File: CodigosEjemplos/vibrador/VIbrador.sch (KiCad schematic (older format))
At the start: 5 parts, among them U1 Pila3,7V, U2 ArduinoNANO, U3 Buzzer, U4 HC-05, U5 Buzzer

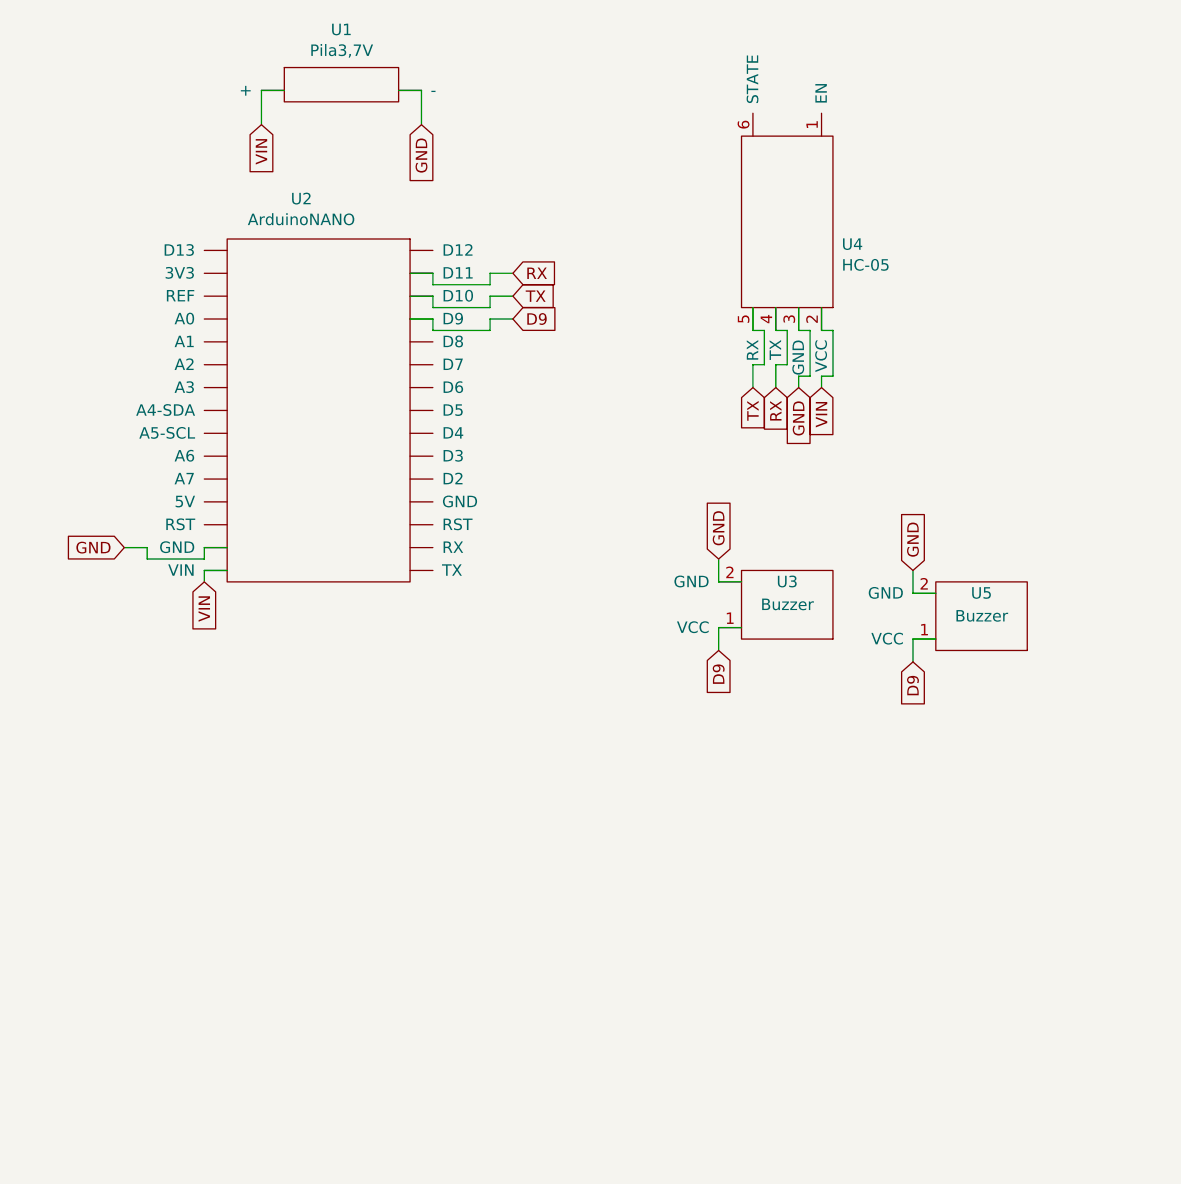
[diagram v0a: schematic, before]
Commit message: Se agregaron los PCB de HC-05, pila (falta completar) y vibrador
Tambien cambie el simbolo de hc-05 ya que le faltaban dos pines
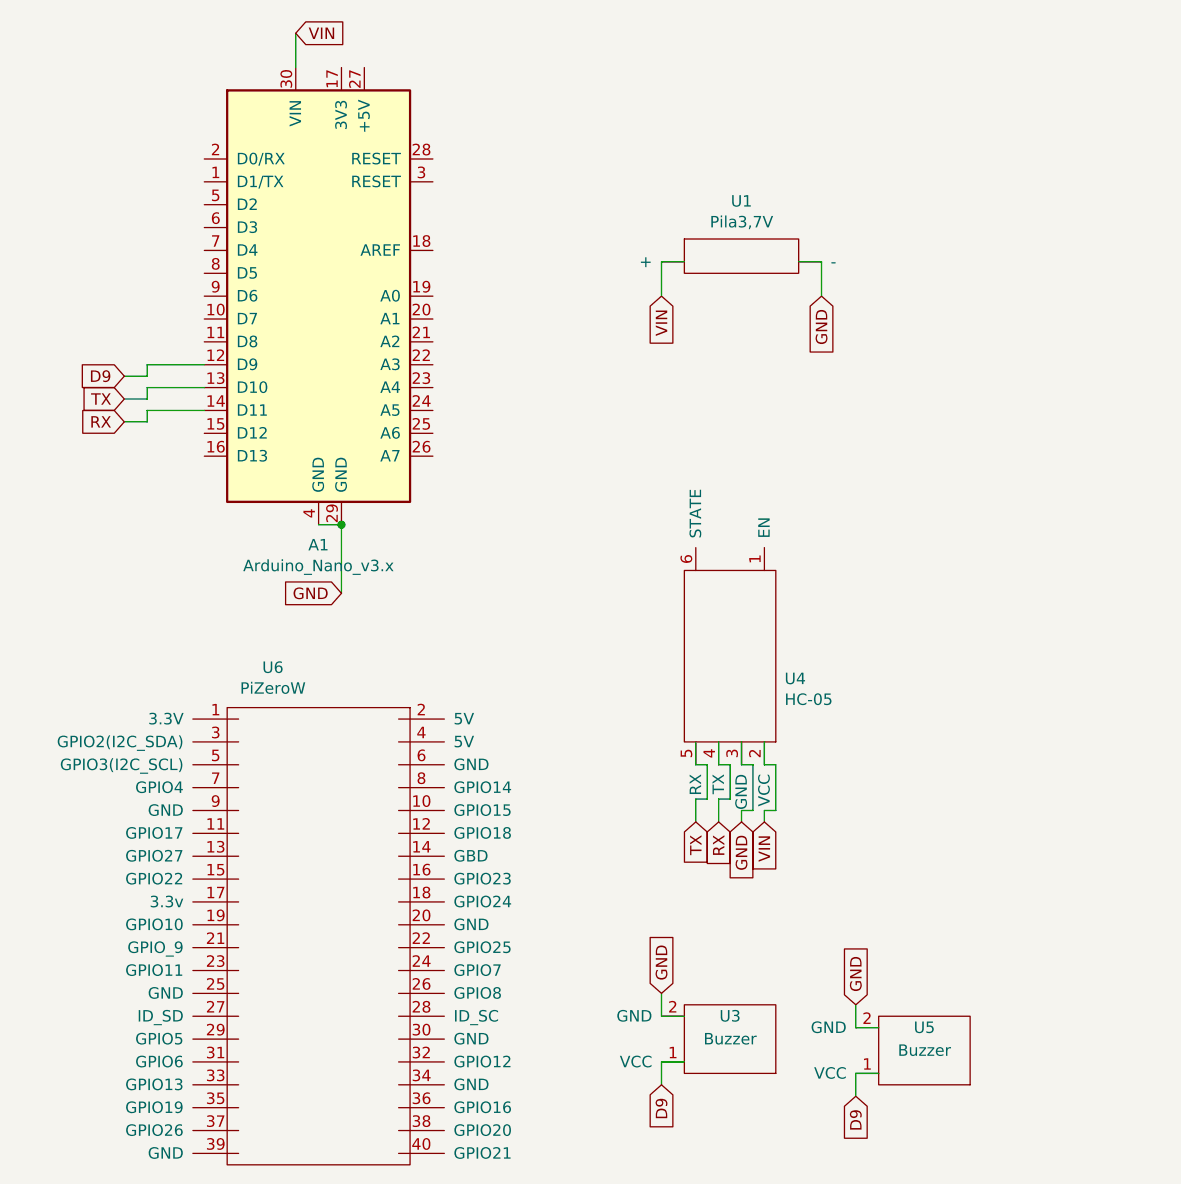
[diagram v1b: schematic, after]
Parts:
- removed U2: ArduinoNANO, Connector_PinHeader_2.54mm:PinHeader_1x15_P2.54mm_Vertical, symbol VIbrador-rescue:ArduinoNANO-Modulos-VIbrador-rescue
- added A1: Arduino_Nano_v3.x, Module:Arduino_Nano, symbol MCU_Module:Arduino_Nano_v3.x
- added U6: PiZeroW, Module:Raspberry_Pi_Zero_Socketed_THT_FaceDown_MountingHoles, symbol VIbrador-rescue:PiZeroW
- U1: footprint (none) -> VibradorPCB:Pila de Litio
- U3, U5: footprint Connector_PinHeader_2.54mm:PinHeader_1x02_P2.54mm_Vertical -> VibradorPCB:Vibrador
- U4: footprint Connector_PinHeader_2.54mm:PinHeader_1x06_P2.54mm_Vertical -> VibradorPCB:HC-05
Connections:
- net D9: now also A1.12 (D9)
- net GND: now also A1.29 (GND), A1.4 (GND)
- net RX: now also A1.14 (D11)
- net TX: now also A1.13 (D10)
- net VIN: now also A1.30 (VIN)
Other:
- moved on the sheet: U1, U3, U4, U5
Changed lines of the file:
@@
 EESchema Schematic File Version 4
-EELAYER 30 0
+LIBS:VIbrador-cache
+EELAYER 29 0
 EELAYER END
 $Descr A4 8268 11693 portrait
@@
 L VIbrador-rescue:HC-05-Modulos-VIbrador-rescue U4
 U 1 1 5E6EC1C3
-P 5000 2200
-F 0 "U4" V 5074 2338 50  0000 L CNN
-F 1 "HC-05" V 5165 2338 50  0000 L CNN
-F 2 "Connector_PinHeader_2.54mm:PinHeader_1x06_P2.54mm_Vertical" H 5000 2200 50  0001 C CNN
-F 3 "" H 5000 2200 50  0001 C CNN
-	1    5000 2200
+P 4750 4100
+F 0 "U4" V 4824 4238 50  0000 L CNN
+F 1 "HC-05" V 4915 4238 50  0000 L CNN
+F 2 "VibradorPCB:HC-05" H 4750 4100 50  0001 C CNN
+F 3 "" H 4750 4100 50  0001 C CNN
+	1    4750 4100
 	0    1    1    0
 $EndComp
@@
 L VIbrador-rescue:Pila3,7V-Modulos-VIbrador-rescue U1
 U 1 1 5E6ECDF3
-P 2900 1550
-F 0 "U1" H 2950 1765 50  0000 C CNN
-F 1 "Pila3,7V" H 2950 1674 50  0000 C CNN
-F 2 "" H 2900 1550 50  0001 C CNN
-F 3 "" H 2900 1550 50  0001 C CNN
-	1    2900 1550
+P 4650 2300
+F 0 "U1" H 4700 2515 50  0000 C CNN
+F 1 "Pila3,7V" H 4700 2424 50  0000 C CNN
+F 2 "VibradorPCB:Pila de Litio" H 4650 2300 50  0001 C CNN
+F 3 "" H 4650 2300 50  0001 C CNN
+	1    4650 2300
 	1    0    0    -1
 $EndComp
-Text GLabel 2600 1750 3    50   Input ~ 0
+Text GLabel 4350 2500 3    50   Input ~ 0
 VIN
-Text GLabel 3300 1750 3    50   Input ~ 0
-GND
-Wire Wire Line
-	3300 1750 3300 1600
-Wire Wire Line
-	3300 1600 3200 1600
-Wire Wire Line
-	2700 1600 2600 1600
-Wire Wire Line
-	2600 1600 2600 1750
-Text GLabel 2350 3750 3    50   Input ~ 0
+Text GLabel 5050 2500 3    50   Input ~ 0
+GND
+Wire Wire Line
+	5050 2500 5050 2350
+Wire Wire Line
+	5050 2350 4950 2350
+Wire Wire Line
+	4450 2350 4350 2350
+Wire Wire Line
+	4350 2350 4350 2500
+Text GLabel 2750 1350 2    50   Input ~ 0
 VIN
-Wire Wire Line
-	2450 3700 2350 3700
-Wire Wire Line
-	2350 3700 2350 3750
-Text GLabel 2000 3600 0    50   Input ~ 0
-GND
-Text GLabel 4750 2900 3    50   Input ~ 0
+Text GLabel 2950 3800 0    50   Input ~ 0
+GND
+Text GLabel 4500 4800 3    50   Input ~ 0
 TX
-Text GLabel 4850 2900 3    50   Input ~ 0
+Text GLabel 4600 4800 3    50   Input ~ 0
 RX
-Text GLabel 4600 4050 3    50   Input ~ 0
+Text GLabel 4350 5950 3    50   Input ~ 0
 D9
 Wire Wire Line
-	4700 3950 4600 3950
-Wire Wire Line
-	4600 3950 4600 4050
-Text GLabel 4600 3650 1    50   Input ~ 0
-GND
-Wire Wire Line
-	4600 3750 4600 3650
-Wire Wire Line
-	4600 3750 4700 3750
-Text GLabel 5050 2900 3    50   Input ~ 0
+	4450 5850 4350 5850
+Wire Wire Line
+	4350 5850 4350 5950
+Text GLabel 4350 5550 1    50   Input ~ 0
+GND
+Wire Wire Line
+	4350 5650 4350 5550
+Wire Wire Line
+	4350 5650 4450 5650
+Text GLabel 4800 4800 3    50   Input ~ 0
 VIN
-Text GLabel 4950 2900 3    50   Input ~ 0
-GND
-Text GLabel 3700 2400 2    50   Input ~ 0
+Text GLabel 4700 4800 3    50   Input ~ 0
+GND
+Text GLabel 2000 3050 0    50   Input ~ 0
 RX
-$Comp
-L VIbrador-rescue:ArduinoNANO-Modulos-VIbrador-rescue U2
-U 1 1 5E6EAAF3
-P 3100 2700
-F 0 "U2" V 2475 2375 50  0000 C CNN
-F 1 "ArduinoNANO" V 2566 2375 50  0000 C CNN
-F 2 "Connector_PinHeader_2.54mm:PinHeader_1x15_P2.54mm_Vertical" H 3100 2700 50  0001 C CNN
-F 3 "" H 3100 2700 50  0001 C CNN
-	1    3100 2700
-	0    1    1    0
-$EndComp
-Wire Wire Line
-	3250 2400 3350 2400
-Wire Wire Line
-	3600 2400 3700 2400
-Text GLabel 3700 2500 2    50   Input ~ 0
+Wire Wire Line
+	2100 3050 2000 3050
+Text GLabel 2000 2950 0    50   Input ~ 0
 TX
-Text GLabel 3700 2600 2    50   Input ~ 0
+Text GLabel 2000 2850 0    50   Input ~ 0
 D9
 Wire Wire Line
-	3600 2400 3600 2450
-Wire Wire Line
-	3600 2450 3350 2450
-Wire Wire Line
-	3350 2450 3350 2400
-Wire Wire Line
-	3350 2500 3350 2550
-Wire Wire Line
-	3350 2550 3600 2550
-Wire Wire Line
-	3600 2550 3600 2500
-Wire Wire Line
-	3600 2500 3700 2500
-Wire Wire Line
-	3700 2600 3600 2600
-Wire Wire Line
-	3600 2600 3600 2650
-Wire Wire Line
-	3600 2650 3350 2650
-Wire Wire Line
-	3350 2650 3350 2600
-Wire Wire Line
-	3350 2600 3250 2600
-Wire Wire Line
-	3250 2500 3350 2500
-Wire Wire Line
-	2450 3600 2350 3600
-Wire Wire Line
-	2350 3600 2350 3650
-Wire Wire Line
-	2350 3650 2100 3650
-Wire Wire Line
-	2100 3650 2100 3600
-Wire Wire Line
-	2100 3600 2000 3600
-Wire Wire Line
-	4750 2550 4750 2650
-Wire Wire Line
-	4750 2650 4800 2650
-Wire Wire Line
-	4800 2650 4800 2800
-Wire Wire Line
-	4800 2800 4750 2800
-Wire Wire Line
-	4750 2800 4750 2900
-Wire Wire Line
-	4850 2900 4850 2800
-Wire Wire Line
-	4850 2800 4900 2800
-Wire Wire Line
-	4900 2800 4900 2650
-Wire Wire Line
-	4900 2650 4850 2650
-Wire Wire Line
-	4850 2650 4850 2550
-Wire Wire Line
-	4950 2550 4950 2650
-Wire Wire Line
-	4950 2650 5000 2650
-Wire Wire Line
-	5000 2650 5000 2850
-Wire Wire Line
-	5000 2850 4950 2850
-Wire Wire Line
-	4950 2850 4950 2900
-Wire Wire Line
-	5050 2550 5050 2650
-Wire Wire Line
-	5050 2650 5100 2650
-Wire Wire Line
-	5100 2650 5100 2850
-Wire Wire Line
-	5100 2850 5050 2850
-Wire Wire Line
-	5050 2850 5050 2900
+	2100 3050 2100 3000
+Wire Wire Line
+	2100 3000 2350 3000
+Wire Wire Line
+	2350 2900 2100 2900
+Wire Wire Line
+	2100 2900 2100 2950
+Wire Wire Line
+	2100 2950 2000 2950
+Wire Wire Line
+	2000 2850 2100 2850
+Wire Wire Line
+	2100 2850 2100 2800
+Wire Wire Line
+	2100 2800 2350 2800
+Wire Wire Line
+	4500 4450 4500 4550
+Wire Wire Line
+	4500 4550 4550 4550
+Wire Wire Line
+	4550 4550 4550 4700
+Wire Wire Line
+	4550 4700 4500 4700
+Wire Wire Line
+	4500 4700 4500 4800
+Wire Wire Line
+	4600 4800 4600 4700
+Wire Wire Line
+	4600 4700 4650 4700
+Wire Wire Line
+	4650 4700 4650 4550
+Wire Wire Line
+	4650 4550 4600 4550
+Wire Wire Line
+	4600 4550 4600 4450
+Wire Wire Line
+	4700 4450 4700 4550
+Wire Wire Line
+	4700 4550 4750 4550
+Wire Wire Line
+	4750 4550 4750 4750
+Wire Wire Line
+	4750 4750 4700 4750
+Wire Wire Line
+	4700 4750 4700 4800
+Wire Wire Line
+	4800 4450 4800 4550
+Wire Wire Line
+	4800 4550 4850 4550
+Wire Wire Line
+	4850 4550 4850 4750
+Wire Wire Line
+	4850 4750 4800 4750
+Wire Wire Line
+	4800 4750 4800 4800
 $Comp
 L VIbrador-rescue:Buzzer-Modulos-VIbrador-rescue U3
 U 1 1 5E6F1D29
-P 4950 3900
-F 0 "U3" H 5000 3750 50  0000 C CNN
-F 1 "Buzzer" H 5000 3850 50  0000 C CNN
-F 2 "Connector_PinHeader_2.54mm:PinHeader_1x02_P2.54mm_Vertical" H 4950 3900 50  0001 C CNN
-F 3 "" H 4950 3900 50  0001 C CNN
-	1    4950 3900
+P 4700 5800
+F 0 "U3" H 4750 5650 50  0000 C CNN
+F 1 "Buzzer" H 4750 5750 50  0000 C CNN
+F 2 "VibradorPCB:Vibrador" H 4700 5800 50  0001 C CNN
+F 3 "" H 4700 5800 50  0001 C CNN
+	1    4700 5800
 	-1   0    0    1
 $EndComp
-Text GLabel 5450 4100 3    50   Input ~ 0
+Text GLabel 5200 6000 3    50   Input ~ 0
 D9
 Wire Wire Line
-	5550 4000 5450 4000
-Wire Wire Line
-	5450 4000 5450 4100
-Text GLabel 5450 3700 1    50   Input ~ 0
-GND
-Wire Wire Line
-	5450 3800 5450 3700
-Wire Wire Line
-	5450 3800 5550 3800
+	5300 5900 5200 5900
+Wire Wire Line
+	5200 5900 5200 6000
+Text GLabel 5200 5600 1    50   Input ~ 0
+GND
+Wire Wire Line
+	5200 5700 5200 5600
+Wire Wire Line
+	5200 5700 5300 5700
 $Comp
 L VIbrador-rescue:Buzzer-Modulos-VIbrador-rescue U5
 U 1 1 5E8A4DBD
-P 5800 3950
-F 0 "U5" H 5850 3800 50  0000 C CNN
-F 1 "Buzzer" H 5850 3900 50  0000 C CNN
-F 2 "Connector_PinHeader_2.54mm:PinHeader_1x02_P2.54mm_Vertical" H 5800 3950 50  0001 C CNN
-F 3 "" H 5800 3950 50  0001 C CNN
-	1    5800 3950
+P 5550 5850
+F 0 "U5" H 5600 5700 50  0000 C CNN
+F 1 "Buzzer" H 5600 5800 50  0000 C CNN
+F 2 "VibradorPCB:Vibrador" H 5550 5850 50  0001 C CNN
+F 3 "" H 5550 5850 50  0001 C CNN
+	1    5550 5850
 	-1   0    0    1
 $EndComp
+$Comp
+L VIbrador-rescue:PiZeroW U6
+U 1 1 5E9167F3
+P 2800 4300
+F 0 "U6" H 2650 4475 50  0000 C CNN
+F 1 "PiZeroW" H 2650 4384 50  0000 C CNN
+F 2 "Module:Raspberry_Pi_Zero_Socketed_THT_FaceDown_MountingHoles" H 2800 4300 50  0001 C CNN
+F 3 "" H 2800 4300 50  0001 C CNN
+	1    2800 4300
+	1    0    0    -1
+$EndComp
+$Comp
+L MCU_Module:Arduino_Nano_v3.x A1
+U 1 1 5E91EE2F
+P 2850 2500
+F 0 "A1" H 2850 1411 50  0000 C CNN
+F 1 "Arduino_Nano_v3.x" H 2850 1320 50  0000 C CNN
+F 2 "Module:Arduino_Nano" H 3000 1550 50  0001 L CNN
+F 3 "http://www.mouser.com/pdfdocs/Gravitech_Arduino_Nano3_0.pdf" H 2850 1500 50  0001 C CNN
+	1    2850 2500
+	1    0    0    -1
+$EndComp
+Wire Wire Line
+	2950 3800 2950 3500
+Wire Wire Line
+	2850 3500 2950 3500
+Connection ~ 2950 3500
+Wire Wire Line
+	2750 1350 2750 1500
 $EndSCHEMATC

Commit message: PCB con StepDown
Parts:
- added U2: StepDown, VibradorPCB:StepDown, symbol VIbrador-rescue:StepDown
- added U7: Pila3,7V-Modulos-VIbrador-rescue, VibradorPCB:Pila de Litio, symbol VIbrador-rescue:Pila3,7V-Modulos-VIbrador-rescue
- A1: symbol MCU_Module:Arduino_Nano_v3.x -> VIbrador-rescue:Arduino_Nano_v3.x-MCU_Module
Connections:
- net GND: no longer U1.~ (-)
- net VIN: no longer U1.~ (-)
- new net: U1.~ (-), U7.~ (-)
- new net IN+: U2.1 (IN+), U7.~ (-)
- new net IN-: U1.~ (-), U2.3 (IN-)
- new net OUT+: U2.2 (OUT+)
- new net OUT-: U2.4 (OUT-)
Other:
- moved on the sheet: U1
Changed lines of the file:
@@
 EESchema Schematic File Version 4
-LIBS:VIbrador-cache
-EELAYER 29 0
+EELAYER 30 0
 EELAYER END
 $Descr A4 8268 11693 portrait
@@
 L VIbrador-rescue:Pila3,7V-Modulos-VIbrador-rescue U1
 U 1 1 5E6ECDF3
-P 4650 2300
-F 0 "U1" H 4700 2515 50  0000 C CNN
-F 1 "Pila3,7V" H 4700 2424 50  0000 C CNN
-F 2 "VibradorPCB:Pila de Litio" H 4650 2300 50  0001 C CNN
-F 3 "" H 4650 2300 50  0001 C CNN
-	1    4650 2300
-	1    0    0    -1
-$EndComp
-Text GLabel 4350 2500 3    50   Input ~ 0
-VIN
-Text GLabel 5050 2500 3    50   Input ~ 0
-GND
-Wire Wire Line
-	5050 2500 5050 2350
-Wire Wire Line
-	5050 2350 4950 2350
+P 4750 2400
+F 0 "U1" H 4800 2615 50  0000 C CNN
+F 1 "Pila3,7V" H 4800 2200 50  0000 C CNN
+F 2 "VibradorPCB:Pila de Litio" H 4750 2400 50  0001 C CNN
+F 3 "" H 4750 2400 50  0001 C CNN
+	1    4750 2400
+	-1   0    0    1
+$EndComp
 Wire Wire Line
 	4450 2350 4350 2350
-Wire Wire Line
-	4350 2350 4350 2500
 Text GLabel 2750 1350 2    50   Input ~ 0
 VIN
@@
 $EndComp
 $Comp
-L MCU_Module:Arduino_Nano_v3.x A1
+L VIbrador-rescue:Arduino_Nano_v3.x-MCU_Module A1
 U 1 1 5E91EE2F
 P 2850 2500
@@
 Wire Wire Line
 	2750 1350 2750 1500
+$Comp
+L VIbrador-rescue:Pila3,7V-Modulos-VIbrador-rescue U7
+U 1 1 5E94B3CF
+P 5750 2400
+F 0 "U7" H 5800 2615 50  0000 C CNN
+F 1 "Pila3,7V-Modulos-VIbrador-rescue" H 5800 2200 50  0000 C CNN
+F 2 "VibradorPCB:Pila de Litio" H 5750 2400 50  0001 C CNN
+F 3 "" H 5750 2400 50  0001 C CNN
+	1    5750 2400
+	-1   0    0    1
+$EndComp
+Wire Wire Line
+	5050 2350 4950 2350
+Wire Wire Line
+	5450 2350 5350 2350
+Wire Wire Line
+	5350 2350 5350 2450
+Wire Wire Line
+	5350 2450 5050 2450
+Wire Wire Line
+	5050 2450 5050 2350
+$Comp
+L VIbrador-rescue:StepDown U2
+U 1 1 5E9524F1
+P 5250 2800
+F 0 "U2" H 5275 3075 50  0000 C CNN
+F 1 "StepDown" H 5275 2984 50  0000 C CNN
+F 2 "VibradorPCB:StepDown" H 5250 2800 50  0001 C CNN
+F 3 "" H 5250 2800 50  0001 C CNN
+	1    5250 2800
+	1    0    0    -1
+$EndComp
+Text GLabel 4800 2850 0    50   Input ~ 0
+IN+
+Text GLabel 6250 2350 2    50   Input ~ 0
+IN+
+Text GLabel 4200 2350 0    50   Input ~ 0
+IN-
+Text GLabel 4800 3050 0    50   Input ~ 0
+IN-
+Wire Wire Line
+	4800 2850 4850 2850
+Wire Wire Line
+	4850 2850 4850 2750
+Wire Wire Line
+	4850 2750 5050 2750
+Wire Wire Line
+	4800 3050 4850 3050
+Wire Wire Line
+	4850 3050 4850 3150
+Wire Wire Line
+	4850 3150 5050 3150
+Wire Wire Line
+	4350 2350 4350 2450
+Wire Wire Line
+	4350 2450 4200 2450
+Wire Wire Line
+	4200 2450 4200 2350
+Wire Wire Line
+	5950 2350 6050 2350
+Wire Wire Line
+	6050 2350 6050 2450
+Wire Wire Line
+	6050 2450 6250 2450
+Wire Wire Line
+	6250 2450 6250 2350
+Text GLabel 5800 2850 2    50   Input ~ 0
+OUT+
+Text GLabel 5800 3050 2    50   Input ~ 0
+OUT-
+Wire Wire Line
+	5800 2850 5650 2850
+Wire Wire Line
+	5650 2850 5650 2750
+Wire Wire Line
+	5650 2750 5450 2750
+Wire Wire Line
+	5450 3150 5650 3150
+Wire Wire Line
+	5650 3150 5650 3050
+Wire Wire Line
+	5650 3050 5800 3050
 $EndSCHEMATC
